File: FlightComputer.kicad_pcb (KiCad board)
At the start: 4 copper layers, 73.7 x 73.7 mm, 92 parts, among them J1 B3B-XH-A, J3 DM3D-SF, J4 12401832E402A, U1 AP62150WU-7TSOT26-WU_DIO, U2 TPS2121RUXR, U4 RP2350_60QFN, Y1 ABM8-272-T3

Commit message: feat: add Brian's logo to bottom silkscreen
Takes the B.Cu logo from PR #8 rather than merging the PR, which
conflicted with c2f85f2 on the same board file (KiCad files don't merge).

Changes from the original: moved B.Cu -> B.SilkS so it doesn't need
clearance from nets or interact with the GND pour, and scaled 0.5x to
8.5 x 10.2 mm. Finest feature is 0.222 mm, above JLCPCB's 0.15 mm silk
minimum. The F.Cu logo from the same PR was left out - it is 44.6 mm
wide and its 0.222 mm detail means it cannot be scaled below 0.68x
without dropping under the silk minimum.

DRC errors unchanged at 6. silk_over_copper unchanged at 134, so it
overlaps no pads. Adds 96 silk_overlap warnings, all of the logo against
itself - inherent to bitmap-converted artwork, cosmetically harmless.

Co-Authored-By: briandai0 <briandai1239@gmail.com>
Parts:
- added G***: LOGO, LOGO, B.SilkS at (135.5, 115.0)

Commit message: chore: reposition logo on bottom silkscreen
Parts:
- G***: moved to F.Cu
- moved G*** 35.0 mm to (170.5, 116.5)

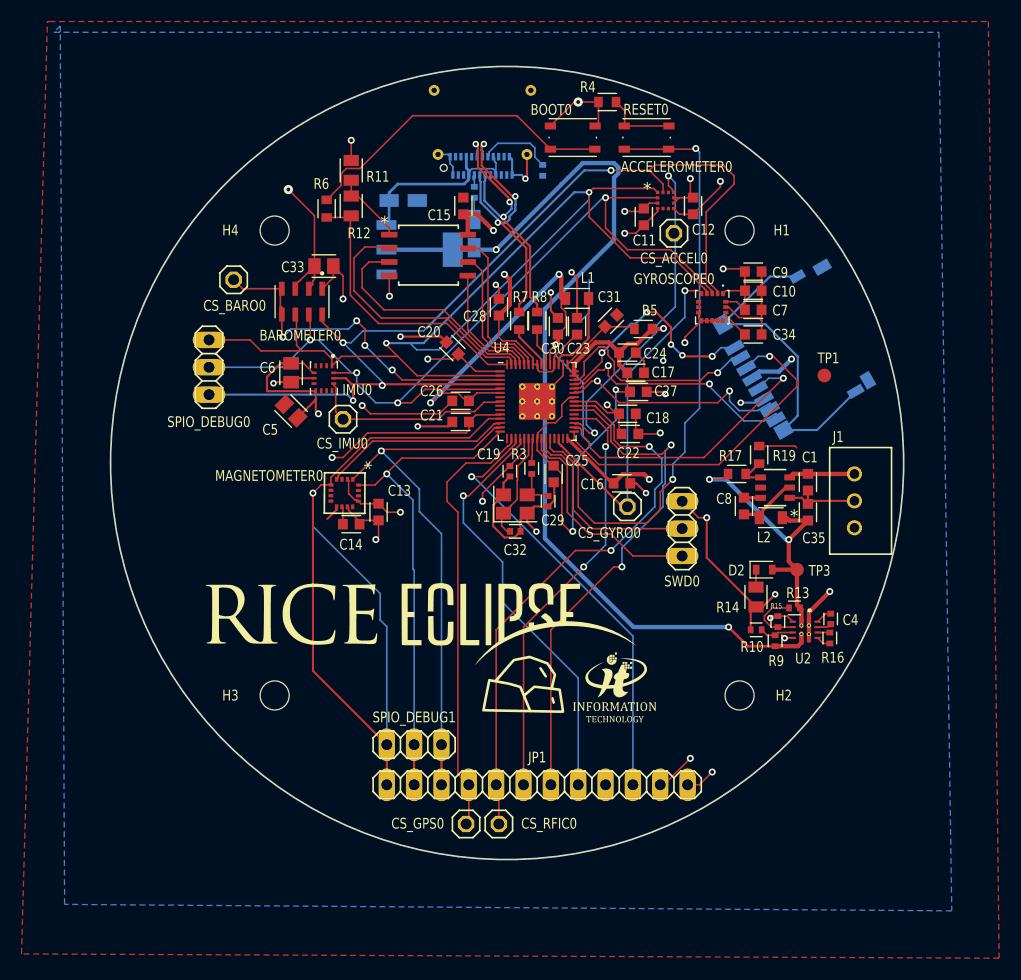
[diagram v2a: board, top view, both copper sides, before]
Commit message: resized board
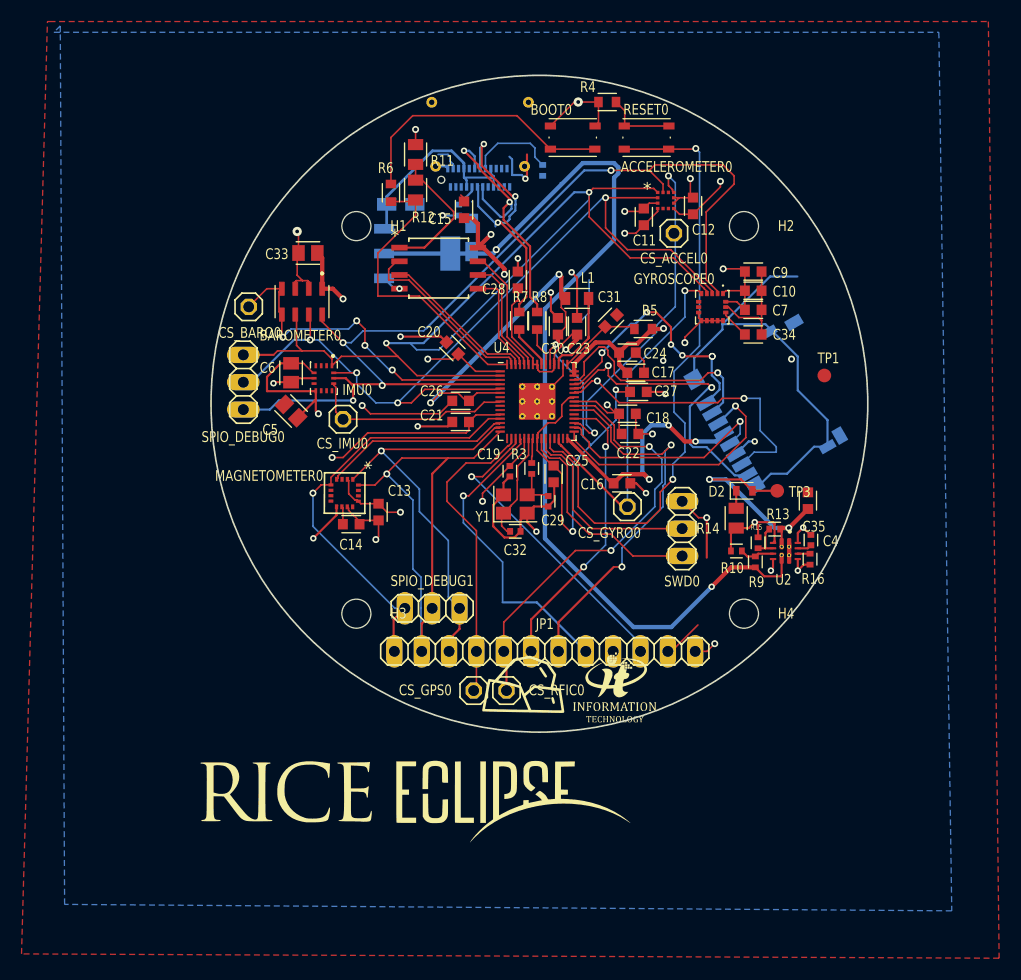
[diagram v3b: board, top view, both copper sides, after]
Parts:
- removed C1: 10uF, FlightComputer:CAPC1608X85
- removed C8: 100nF, FlightComputer:CAPC1608X85
- removed the H4 at (126.9, 83.4)
- removed J1: B3B-XH-A, FlightComputer:B3B-XH-A
- removed L2: 3.3uH, FlightComputer:INDC2009X120
- removed R17: 31.6k, FlightComputer:RESC1608X60
- removed R19: 10k, FlightComputer:RESC1608X60
- removed U1: AP62150WU-7TSOT26-WU_DIO, FlightComputer:TSOT26-WU_DIO
- added H1: MountingHole, FlightComputer:MOUNTINGHOLE_MOUNTINGHOLE_2.7MM_M2.5, F.Cu at (134.5, 83.0)
- moved H2 43.6 mm to (170.5, 83.0)
- moved H4 35.6 mm to (170.5, 119.0)
- moved G*** 20.2 mm to (178.5, 135.0)
- moved G*** 16.5 mm to (140.0, 136.5)
- moved G*** 14.6 mm to (121.5, 117.0)
- moved SPIO_DEBUG1 12.8 mm to (141.5, 118.5)
- moved JP1 12.4 mm to (152.0, 122.5)
- moved CS_GPS0 12.4 mm to (145.4, 126.1)
- moved CS_RFIC0 12.4 mm to (148.4, 126.1)
- moved H3 10.7 mm to (134.5, 119.0)
- moved R14 7.55 mm to (169.8, 110.1)
- moved R10 7.55 mm to (169.8, 113.2)
- moved R15 7.55 mm to (171.8, 112.4)
- moved R16 7.55 mm to (176.6, 113.9)
- moved U2 7.55 mm to (174.3, 113.2)
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- renumbered H1 to H4
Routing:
- net /MISO1: track 80.5 -> 39.9 mm
- net GND: track 169.0 -> 150.5 mm, vias 26 -> 29
- net /SCLK1: track 52.7 -> 37.7 mm, vias 1 -> 2
- net /CS_RFIC: track 53.3 -> 40.6 mm
- net /RF_GPIO2: track 48.5 -> 35.8 mm
- net /RF_GPIO0: track 39.7 -> 27.0 mm
- net /CS_GPS: track 40.6 -> 28.5 mm
- net /LNA_EN_LP: track 40.8 -> 28.7 mm
- net /RF_GPIO3: track 39.1 -> 28.9 mm, vias 1 -> 2
- net Net-(J3-SHIELD-PadS1): track 32.6 -> 41.0 mm
- net /SDIO_CMD: track 32.1 -> 24.3 mm
- net /QSPI_SD2: track 22.0 -> 14.5 mm
- net /QSPI_SD1: track 24.5 -> 17.2 mm
- net +3V3: track 153.5 -> 160.4 mm, vias 18 -> 20
- net /+7.4V: track 6.16 -> 0.00 mm
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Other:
- board size 73.7 x 73.7 mm -> 61 x 61 mm

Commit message: fix: recentre mounting holes and bring logos inside the 61mm outline
Follow-up to PR #10.

Mounting holes: the 36mm square was offset 1.8mm from the board centre, so
the four distances spread 23.69-27.23mm and the board would sit eccentric on
the av-bay rods. Now all four at 25.456mm, concentric. The SIZE is still a
placeholder - the real bolt pattern is the av-bay rod spacing, pending
mechanical.

Logos: four of five had copper outside the outline (by 0.6 to 19.4mm).
Moved inside. The 39.9mm-wide one needed recentring rather than pulling
radially inward.

Remaining DRC (2, both known):
- hole_clearance: H2 sits 0.215mm from /SCLK0, needs 0.25mm. An artifact of
  the placeholder pattern; resolves when the real spacing lands.
- diff_pair_uncoupled_length: 7.83mm against a 6mm rule. Measured the actual
  skew: 1.167mm mismatch = 8.0ps, which is 0.0096% of the Full-Speed bit
  period and TIGHTER than the 1.56mm/10.7ps that justified the earlier 5->6mm
  relaxation. The rule guards against High-Speed designs, where the same
  7.83mm would be 10.7% of a 500ps edge. Left visible pending a decision.

NOT fixed, flagged for a human: the 25,356-point logo at (121.5, 117.0) is
20.1mm outside the outline. It needs re-exporting from source at lower detail
rather than moving - it is ~745KB, about a third of the board file.
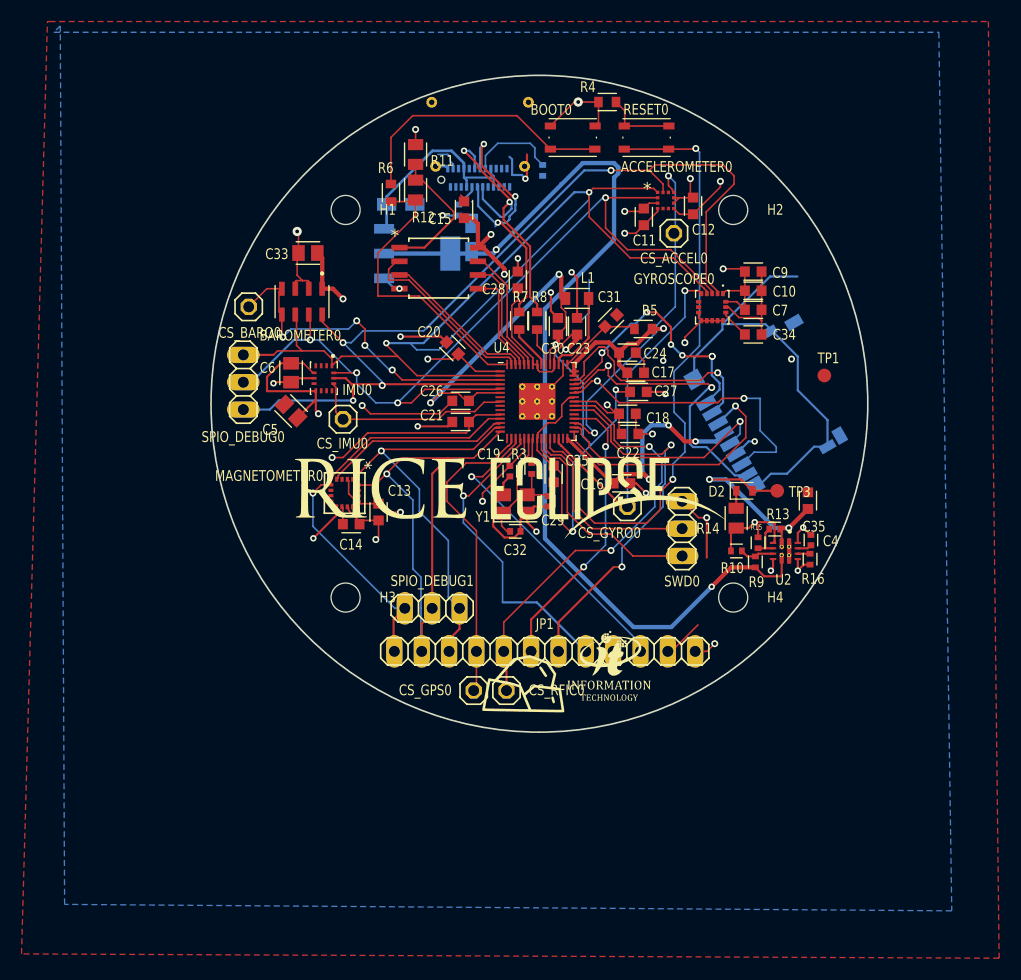
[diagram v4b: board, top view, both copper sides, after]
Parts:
- moved G*** 29.5 mm to (148.8, 108.3)
- moved G*** 20.1 mm to (166.3, 119.0)
- moved G*** 2.07 mm to (158.0, 124.0)
- moved H1 1.80 mm to (133.5, 81.5)
- moved H2 1.80 mm to (169.5, 81.5)
- moved H3 1.80 mm to (133.5, 117.5)
- moved H4 1.80 mm to (169.5, 117.5)
- moved G*** 0.05 mm to (150.0, 125.4)
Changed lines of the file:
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@@
 	(footprint "LOGO"
 		(layer "F.Cu")
-		(at 178.5 135 180)
+		(at 166.3230 118.9895 180)
 		(property "Reference" "G***"
 			(at 0 0 0)
@@
 	(footprint "FlightComputer:MOUNTINGHOLE_MOUNTINGHOLE_2.7MM_M2.5"
 		(layer "F.Cu")
-		(at 134.5 83)
+		(at 133.5000 81.5000)
 		(descr "Mounting Hole 2.7mm, no annular, M2.5")
 		(property "Reference" "H1"
@@
 	(footprint "FlightComputer:MOUNTINGHOLE_MOUNTINGHOLE_2.7MM_M2.5"
 		(layer "F.Cu")
-		(at 170.5 119)
+		(at 169.5000 117.5000)
 		(descr "Mounting Hole 2.7mm, no annular, M2.5")
 		(property "Reference" "H4"
@@
 	(footprint "FlightComputer:MOUNTINGHOLE_MOUNTINGHOLE_2.7MM_M2.5"
 		(layer "F.Cu")
-		(at 170.5 83)
+		(at 169.5000 81.5000)
 		(descr "Mounting Hole 2.7mm, no annular, M2.5")
 		(property "Reference" "H2"
@@
 	(footprint "LOGO"
 		(layer "F.Cu")
-		(at 158.5 126)
+		(at 157.9712 123.9981)
 		(property "Reference" "G***"
 			(at 0 0 0)
@@
 	(footprint "LOGO"
 		(layer "F.Cu")
-		(at 140 136.5)
+		(at 148.7741 108.3006)
 		(property "Reference" "G***"
 			(at 0 0 0)
@@
 	(footprint "LOGO"
 		(layer "F.Cu")
-		(at 150 125.5)
+		(at 150.0030 125.4472)
 		(property "Reference" "G***"
 			(at 0 0 0)
@@
 	(footprint "FlightComputer:MOUNTINGHOLE_MOUNTINGHOLE_2.7MM_M2.5"
 		(layer "F.Cu")
-		(at 134.5 119)
+		(at 133.5000 117.5000)
 		(descr "Mounting Hole 2.7mm, no annular, M2.5")
 		(property "Reference" "H3"

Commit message: cleaned up some stuff...
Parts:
- moved G*** 29.0 mm to (152.5, 79.5)
- moved G*** 22.6 mm to (141.5, 106.5)
- moved G*** 10.1 mm to (152.0, 115.5)
- moved G*** 6.68 mm to (159.5, 117.5)
- moved C15 1.41 mm to (145.5, 82.5)
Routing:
- net Net-(J3-SHIELD-PadS1): track 41.0 -> 31.1 mm
- net +3V3: track 160.4 -> 152.6 mm, vias 20 -> 18
- net /SDIO_D3: track 23.2 -> 18.8 mm
- net /SCLK0: track 95.3 -> 91.8 mm
- net unconnected-(J4-RX1+-PadB11): track 2.48 -> 0.04 mm
- net /SDIO_D1: track 27.9 -> 25.9 mm, vias 2 -> 1
- net Net-(J4-CC2): track 8.32 -> 6.59 mm
- net GND: track 150.5 -> 149.0 mm
- net /SDIO_D2: track 23.9 -> 25.0 mm, vias 6 -> 3
- net /SDIO_D0: track 28.0 -> 27.2 mm, vias 2 -> 1
- net /USB_P: track 26.9 -> 27.5 mm
- net /USB_N: track 26.2 -> 26.8 mm
- net /+3V3_USB: track 92.5 -> 92.7 mm, vias 2 -> 1
- net /SCLK1: vias 2 -> 1
- net /RF_GPIO3: vias 2 -> 1

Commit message: board with hole
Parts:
- moved J4 50.1 mm to (159.8, 122.5), turned to 180 degrees
- moved C5 32.4 mm to (144.5, 72.0), turned to -135 degrees
- moved SPIO_DEBUG0 27.2 mm to (139.7, 75.3), turned to -135 degrees
- moved CS_BARO0 27.1 mm to (149.1, 79.0), turned to -45 degrees
- moved CS_IMU0 25.1 mm to (147.6, 80.4), turned to 45 degrees
- moved C16 24.3 mm to (134.9, 105.8)
- moved C28 24.3 mm to (125.9, 93.7)
- moved C17 23.6 mm to (136.9, 98.2)
- moved C18 23.4 mm to (136.4, 101.8)
- moved C22 23.4 mm to (136.6, 103.6)
- moved C27 23.4 mm to (137.4, 99.7)
- moved C24 23.2 mm to (136.6, 96.5)
- moved R5 21.9 mm to (139.3, 94.8)
- moved C25 21.2 mm to (131.6, 106.5)
- moved C33 21.1 mm to (147.8, 74.2), turned to 135 degrees
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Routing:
- net GND: track 149.0 -> 42.3 mm, vias 29 -> 22
- net /MISO0: track 104.5 -> 0.74 mm, vias 2 -> 0
- net /SCLK0: track 91.8 -> 2.49 mm, vias 4 -> 0
- net /+3V3_USB: track 92.7 -> 9.25 mm
- net /MOSI0: track 81.2 -> 0.22 mm, vias 4 -> 0
- net +3V3: track 152.6 -> 71.7 mm, vias 18 -> 0
- net +1V1: track 76.9 -> 12.8 mm, vias 5 -> 0
- net /MOSI1: track 52.0 -> 4.50 mm, vias 1 -> 0
- net /RUN: track 59.4 -> 19.5 mm, vias 2 -> 0
- net /MISO1: track 39.9 -> 4.46 mm, vias 1 -> 0
- net /CS_RFIC: track 40.6 -> 6.45 mm, vias 2 -> 0
- net /SCLK1: track 37.7 -> 4.40 mm, vias 1 -> 0
- net /RF_GPIO2: track 35.8 -> 2.71 mm, vias 2 -> 0
- net /CS_BARO: track 32.7 -> 0.00 mm, vias 4 -> 0
- net /CS_ACCEL: track 32.1 -> 0.31 mm, vias 2 -> 0
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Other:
- outline, holes or cut-outs redrawn
